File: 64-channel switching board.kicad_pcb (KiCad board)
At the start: 2 copper layers, 45.6 x 64.8 mm, 69 parts, among them P1 CONN_01X01, P10 CONN_01X01, P11 CONN_01X01, P12 CONN_01X01, P13 CONN_01X01, P14 CONN_01X01, P15 CONN_01X01, P16 CONN_01X01, P17 CONN_01X01, P18 CONN_01X01, P19 CONN_01X01, P2 CONN_01X01, P20 CONN_01X01, P21 CONN_01X01, P22 CONN_01X01, P23 CONN_01X01, P24 CONN_01X01, P25 CONN_01X01, P26 CONN_01X01, P27 CONN_01X01, P28 CONN_01X01, P29 CONN_01X01, P3 CONN_01X01, P30 CONN_01X01, P31 CONN_01X01, P32 CONN_01X01, P33 CONN_01X01, P34 CONN_01X01, P35 CONN_01X01, P36 CONN_01X01, P37 CONN_01X01, P38 CONN_01X01, P39 CONN_01X01, P4 CONN_01X01, P40 CONN_01X01, P41 CONN_01X01, P42 CONN_01X01, P43 CONN_01X01, P44 CONN_01X01, P45 CONN_01X01, P46 CONN_01X01, P47 CONN_01X01, P48 CONN_01X01, P49 CONN_01X01, P5 CONN_01X01, P50 CONN_01X01, P51 CONN_01X01, P52 CONN_01X01, P53 CONN_01X01, P54 CONN_01X01, P55 CONN_01X01, P56 CONN_01X01, P57 CONN_01X01, P58 CONN_01X01, P59 CONN_01X01, P6 CONN_01X01, P60 CONN_01X01, P61 CONN_01X01, P62 CONN_01X01, P63 CONN_01X01, P64 CONN_01X01, P65 CONN_01X10, P66 CONN_01X02, P7 CONN_01X01, P8 CONN_01X01, P9 CONN_01X01, U1 HV507

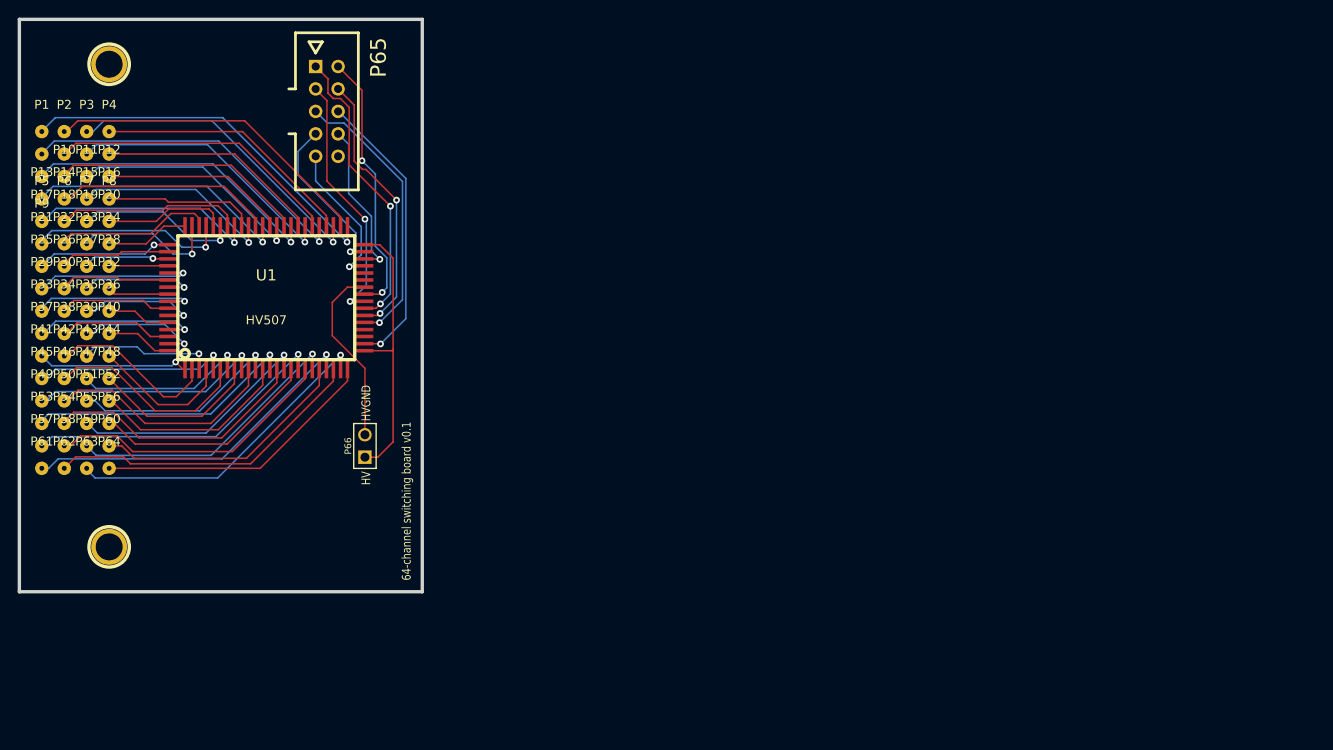
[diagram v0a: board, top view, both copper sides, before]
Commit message: Updated schematic and pcb to have 64 resistors and capacitors. Also added a version with 40 pin connector
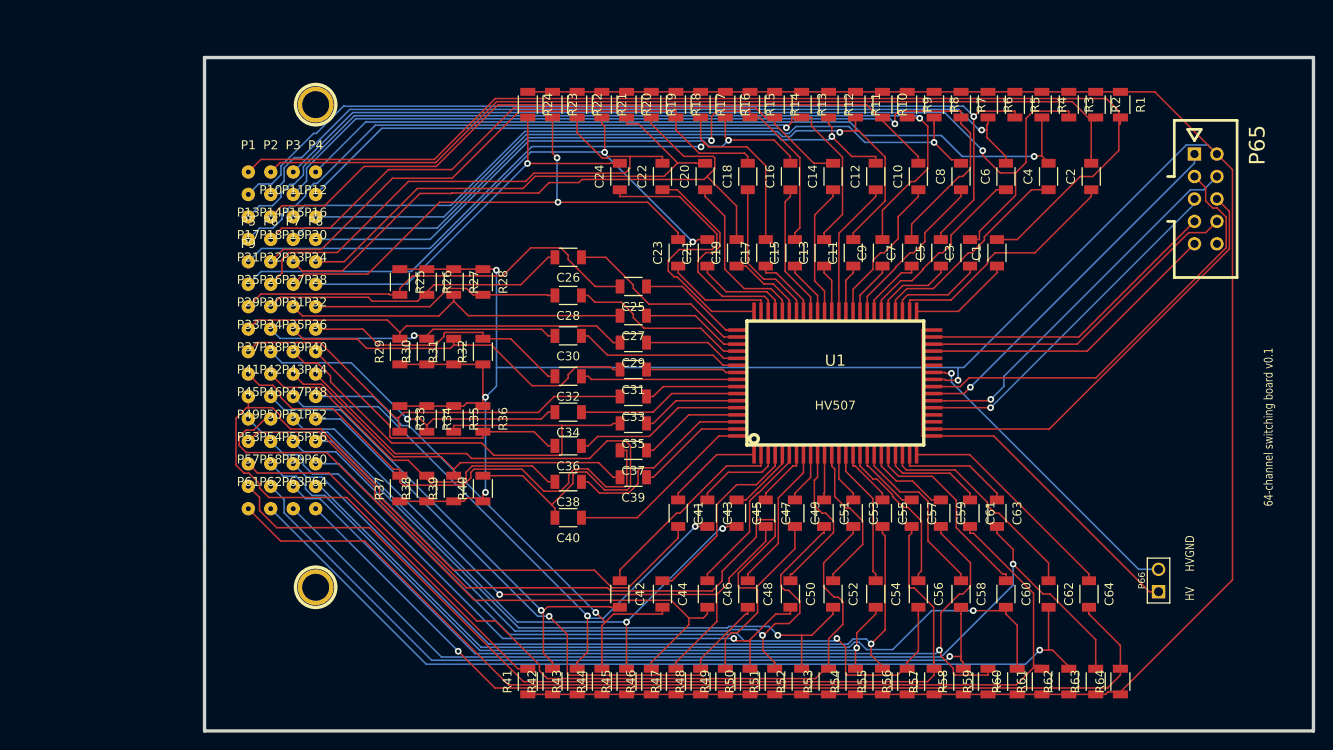
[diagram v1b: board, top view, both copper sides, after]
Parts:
- added C1: 3nF, Capacitors_SMD:C_1206, F.Cu at (123.2, 38.9)
- added C10: 3nF, Capacitors_SMD:C_1206, F.Cu at (114.3, 30.2)
- added C11: 3nF, Capacitors_SMD:C_1206, F.Cu at (106.9, 38.9)
- added C12: 3nF, Capacitors_SMD:C_1206, F.Cu at (109.5, 30.2)
- added C13: 3nF, Capacitors_SMD:C_1206, F.Cu at (103.6, 38.9)
- added C14: 3nF, Capacitors_SMD:C_1206, F.Cu at (104.6, 30.2)
- added C15: 3nF, Capacitors_SMD:C_1206, F.Cu at (100.3, 38.9)
- added C16: 3nF, Capacitors_SMD:C_1206, F.Cu at (99.8, 30.2)
- added C17: 3nF, Capacitors_SMD:C_1206, F.Cu at (97.0, 38.9)
- added C18: 3nF, Capacitors_SMD:C_1206, F.Cu at (95.0, 30.2)
- added C19: 3nF, Capacitors_SMD:C_1206, F.Cu at (93.7, 38.9)
- added C2: 3nF, Capacitors_SMD:C_1206, F.Cu at (133.9, 30.2)
- added C20: 3nF, Capacitors_SMD:C_1206, F.Cu at (90.2, 30.2)
- added C21: 3nF, Capacitors_SMD:C_1206, F.Cu at (90.4, 38.9)
- added C22: 3nF, Capacitors_SMD:C_1206, F.Cu at (85.3, 30.2)
- added C23: 3nF, Capacitors_SMD:C_1206, F.Cu at (87.1, 38.9)
- added C24: 3nF, Capacitors_SMD:C_1206, F.Cu at (80.5, 30.2)
- added C25: 3nF, Capacitors_SMD:C_1206, F.Cu at (82.0, 42.7)
- added C26: 3nF, Capacitors_SMD:C_1206, F.Cu at (74.7, 39.4)
- added C27: 3nF, Capacitors_SMD:C_1206, F.Cu at (82.0, 46.0)
- added C28: 3nF, Capacitors_SMD:C_1206, F.Cu at (74.7, 43.7)
- added C29: 3nF, Capacitors_SMD:C_1206, F.Cu at (82.0, 49.0)
- added C3: 3nF, Capacitors_SMD:C_1206, F.Cu at (120.1, 38.9)
- added C30: 3nF, Capacitors_SMD:C_1206, F.Cu at (74.7, 48.3)
- added C31: 3nF, Capacitors_SMD:C_1206, F.Cu at (82.0, 52.1)
- added C32: 3nF, Capacitors_SMD:C_1206, F.Cu at (74.7, 52.8)
- added C33: 3nF, Capacitors_SMD:C_1206, F.Cu at (82.0, 55.1)
- added C34: 3nF, Capacitors_SMD:C_1206, F.Cu at (74.7, 56.9)
- added C35: 3nF, Capacitors_SMD:C_1206, F.Cu at (82.0, 58.2)
- added C36: 3nF, Capacitors_SMD:C_1206, F.Cu at (74.7, 60.7)
- added C37: 3nF, Capacitors_SMD:C_1206, F.Cu at (82.0, 61.2)
- added C38: 3nF, Capacitors_SMD:C_1206, F.Cu at (74.7, 64.8)
- added C39: 3nF, Capacitors_SMD:C_1206, F.Cu at (82.0, 64.3)
- added C4: 3nF, Capacitors_SMD:C_1206, F.Cu at (129.0, 30.2)
- added C40: 3nF, Capacitors_SMD:C_1206, F.Cu at (74.7, 68.8)
- added C41: 3nF, Capacitors_SMD:C_1206, F.Cu at (87.1, 68.3)
- added C42: 3nF, Capacitors_SMD:C_1206, F.Cu at (80.5, 77.5)
- added C43: 3nF, Capacitors_SMD:C_1206, F.Cu at (90.4, 68.3)
- added C44: 3nF, Capacitors_SMD:C_1206, F.Cu at (85.3, 77.5)
- added C45: 3nF, Capacitors_SMD:C_1206, F.Cu at (93.7, 68.3)
- added C46: 3nF, Capacitors_SMD:C_1206, F.Cu at (90.4, 77.5)
- added C47: 3nF, Capacitors_SMD:C_1206, F.Cu at (97.0, 68.3)
- added C48: 3nF, Capacitors_SMD:C_1206, F.Cu at (95.0, 77.5)
- added C49: 3nF, Capacitors_SMD:C_1206, F.Cu at (100.3, 68.3)
- added C5: 3nF, Capacitors_SMD:C_1206, F.Cu at (116.8, 38.9)
- added C50: 3nF, Capacitors_SMD:C_1206, F.Cu at (99.8, 77.5)
- added C51: 3nF, Capacitors_SMD:C_1206, F.Cu at (103.6, 68.3)
- added C52: 3nF, Capacitors_SMD:C_1206, F.Cu at (104.6, 77.5)
- added C53: 3nF, Capacitors_SMD:C_1206, F.Cu at (106.9, 68.3)
- added C54: 3nF, Capacitors_SMD:C_1206, F.Cu at (109.5, 77.5)
- added C55: 3nF, Capacitors_SMD:C_1206, F.Cu at (110.2, 68.3)
- added C56: 3nF, Capacitors_SMD:C_1206, F.Cu at (114.3, 77.5)
- added C57: 3nF, Capacitors_SMD:C_1206, F.Cu at (113.5, 68.3)
- added C58: 3nF, Capacitors_SMD:C_1206, F.Cu at (119.1, 77.5)
- added C59: 3nF, Capacitors_SMD:C_1206, F.Cu at (116.8, 68.3)
- added C6: 3nF, Capacitors_SMD:C_1206, F.Cu at (124.2, 30.2)
- added C60: 3nF, Capacitors_SMD:C_1206, F.Cu at (124.2, 77.5)
- added C61: 3nF, Capacitors_SMD:C_1206, F.Cu at (120.1, 68.3)
- added C62: 3nF, Capacitors_SMD:C_1206, F.Cu at (129.0, 77.5)
- added C63: 3nF, Capacitors_SMD:C_1206, F.Cu at (123.2, 68.3)
- added C64: 3nF, Capacitors_SMD:C_1206, F.Cu at (133.6, 77.5)
- added C7: 3nF, Capacitors_SMD:C_1206, F.Cu at (113.5, 38.9)
- added C8: 3nF, Capacitors_SMD:C_1206, F.Cu at (119.1, 30.2)
- added C9: 3nF, Capacitors_SMD:C_1206, F.Cu at (110.2, 38.9)
- added R1: 510k, Resistors_SMD:R_1206, F.Cu at (137.2, 22.1)
- added R10: 510k, Resistors_SMD:R_1206, F.Cu at (110.2, 22.1)
- added R11: 510k, Resistors_SMD:R_1206, F.Cu at (107.2, 22.1)
- added R12: 510k, Resistors_SMD:R_1206, F.Cu at (104.1, 22.1)
- added R13: 510k, Resistors_SMD:R_1206, F.Cu at (101.1, 22.1)
- added R14: 510k, Resistors_SMD:R_1206, F.Cu at (98.0, 22.1)
- added R15: 510k, Resistors_SMD:R_1206, F.Cu at (95.2, 22.1)
- added R16: 510k, Resistors_SMD:R_1206, F.Cu at (92.5, 22.1)
- added R17: 510k, Resistors_SMD:R_1206, F.Cu at (89.7, 22.1)
- added R18: 510k, Resistors_SMD:R_1206, F.Cu at (86.9, 22.1)
- added R19: 510k, Resistors_SMD:R_1206, F.Cu at (84.1, 22.1)
- added R2: 510k, Resistors_SMD:R_1206, F.Cu at (134.4, 22.1)
- added R20: 510k, Resistors_SMD:R_1206, F.Cu at (81.3, 22.1)
- added R21: 510k, Resistors_SMD:R_1206, F.Cu at (78.5, 22.1)
- added R22: 510k, Resistors_SMD:R_1206, F.Cu at (75.7, 22.1)
- added R23: 510k, Resistors_SMD:R_1206, F.Cu at (72.9, 22.1)
- added R24: 510k, Resistors_SMD:R_1206, F.Cu at (70.1, 22.1)
- added R25: 510k, Resistors_SMD:R_1206, F.Cu at (55.6, 42.2)
- added R26: 510k, Resistors_SMD:R_1206, F.Cu at (58.7, 42.2)
- added R27: 510k, Resistors_SMD:R_1206, F.Cu at (61.7, 42.2)
- added R28: 510k, Resistors_SMD:R_1206, F.Cu at (65.0, 42.2)
- added R29: 510k, Resistors_SMD:R_1206, F.Cu at (55.6, 50.0)
- added R3: 510k, Resistors_SMD:R_1206, F.Cu at (131.3, 22.1)
- added R30: 510k, Resistors_SMD:R_1206, F.Cu at (58.7, 50.0)
- added R31: 510k, Resistors_SMD:R_1206, F.Cu at (61.7, 50.0)
- added R32: 510k, Resistors_SMD:R_1206, F.Cu at (65.0, 50.0)
- added R33: 510k, Resistors_SMD:R_1206, F.Cu at (55.6, 57.7)
- added R34: 510k, Resistors_SMD:R_1206, F.Cu at (58.7, 57.7)
- added R35: 510k, Resistors_SMD:R_1206, F.Cu at (61.7, 57.7)
- added R36: 510k, Resistors_SMD:R_1206, F.Cu at (65.0, 57.7)
- added R37: 510k, Resistors_SMD:R_1206, F.Cu at (55.6, 65.5)
- added R38: 510k, Resistors_SMD:R_1206, F.Cu at (58.7, 65.5)
- added R39: 510k, Resistors_SMD:R_1206, F.Cu at (61.7, 65.5)
- added R4: 510k, Resistors_SMD:R_1206, F.Cu at (128.3, 22.1)
- added R40: 510k, Resistors_SMD:R_1206, F.Cu at (65.0, 65.5)
- added R41: 510k, Resistors_SMD:R_1206, F.Cu at (70.1, 87.4)
- added R42: 510k, Resistors_SMD:R_1206, F.Cu at (72.9, 87.4)
- added R43: 510k, Resistors_SMD:R_1206, F.Cu at (75.7, 87.4)
- added R44: 510k, Resistors_SMD:R_1206, F.Cu at (78.5, 87.4)
- added R45: 510k, Resistors_SMD:R_1206, F.Cu at (81.3, 87.4)
- added R46: 510k, Resistors_SMD:R_1206, F.Cu at (84.1, 87.4)
- added R47: 510k, Resistors_SMD:R_1206, F.Cu at (86.9, 87.4)
- added R48: 510k, Resistors_SMD:R_1206, F.Cu at (89.7, 87.4)
- added R49: 510k, Resistors_SMD:R_1206, F.Cu at (92.5, 87.4)
- added R5: 510k, Resistors_SMD:R_1206, F.Cu at (125.2, 22.1)
- added R50: 510k, Resistors_SMD:R_1206, F.Cu at (95.2, 87.4)
- added R51: 510k, Resistors_SMD:R_1206, F.Cu at (98.0, 87.4)
- added R52: 510k, Resistors_SMD:R_1206, F.Cu at (101.1, 87.4)
- added R53: 510k, Resistors_SMD:R_1206, F.Cu at (104.1, 87.4)
- added R54: 510k, Resistors_SMD:R_1206, F.Cu at (107.2, 87.4)
- added R55: 510k, Resistors_SMD:R_1206, F.Cu at (110.2, 87.4)
- added R56: 510k, Resistors_SMD:R_1206, F.Cu at (113.0, 87.4)
- added R57: 510k, Resistors_SMD:R_1206, F.Cu at (116.1, 87.4)
- added R58: 510k, Resistors_SMD:R_1206, F.Cu at (119.4, 87.4)
- added R59: 510k, Resistors_SMD:R_1206, F.Cu at (122.2, 87.4)
- added R6: 510k, Resistors_SMD:R_1206, F.Cu at (122.2, 22.1)
- added R60: 510k, Resistors_SMD:R_1206, F.Cu at (125.5, 87.4)
- added R61: 510k, Resistors_SMD:R_1206, F.Cu at (128.3, 87.4)
- added R62: 510k, Resistors_SMD:R_1206, F.Cu at (131.3, 87.4)
- added R63: 510k, Resistors_SMD:R_1206, F.Cu at (134.4, 87.4)
- added R64: 510k, Resistors_SMD:R_1206, F.Cu at (137.2, 87.4)
- added R7: 510k, Resistors_SMD:R_1206, F.Cu at (119.1, 22.1)
- added R8: 510k, Resistors_SMD:R_1206, F.Cu at (116.1, 22.1)
- added R9: 510k, Resistors_SMD:R_1206, F.Cu at (113.0, 22.1)
- moved P65 99.9 mm to (146.8, 32.8)
- moved P66 91.1 mm to (141.5, 75.9)
- moved U1 65.1 mm to (104.9, 53.6)
- moved P1 23.8 mm to (38.5, 29.7)
- moved P10 23.8 mm to (41.0, 34.8)
- moved P13 23.8 mm to (38.5, 37.3)
- moved P14 23.8 mm to (41.0, 37.3)
- moved P17 23.8 mm to (38.5, 39.9)
- moved P18 23.8 mm to (41.0, 39.9)
- moved P2 23.8 mm to (41.0, 29.7)
- moved P21 23.8 mm to (38.5, 42.4)
- moved P22 23.8 mm to (41.0, 42.4)
- moved P25 23.8 mm to (38.5, 45.0)
- moved P26 23.8 mm to (41.0, 45.0)
- moved P29 23.8 mm to (38.5, 47.5)
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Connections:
- P1 pad 1: Net-(P1-Pad1) -> Net-(C1-Pad2)
- P10 pad 1: Net-(P10-Pad1) -> Net-(C10-Pad2)
- P11 pad 1: Net-(P11-Pad1) -> Net-(C11-Pad2)
- P12 pad 1: Net-(P12-Pad1) -> Net-(C12-Pad2)
- P13 pad 1: Net-(P13-Pad1) -> Net-(C13-Pad2)
- P14 pad 1: Net-(P14-Pad1) -> Net-(C14-Pad2)
- P15 pad 1: Net-(P15-Pad1) -> Net-(C15-Pad2)
- P16 pad 1: Net-(P16-Pad1) -> Net-(C16-Pad2)
- P17 pad 1: Net-(P17-Pad1) -> Net-(C17-Pad2)
- P18 pad 1: Net-(P18-Pad1) -> Net-(C18-Pad2)
- P19 pad 1: Net-(P19-Pad1) -> Net-(C19-Pad2)
- P2 pad 1: Net-(P2-Pad1) -> Net-(C2-Pad2)
- P20 pad 1: Net-(P20-Pad1) -> Net-(C20-Pad2)
- P21 pad 1: Net-(P21-Pad1) -> Net-(C21-Pad2)
- P22 pad 1: Net-(P22-Pad1) -> Net-(C22-Pad2)
- P23 pad 1: Net-(P23-Pad1) -> Net-(C23-Pad2)
- P24 pad 1: Net-(P24-Pad1) -> Net-(C24-Pad2)
- P25 pad 1: Net-(P25-Pad1) -> Net-(C25-Pad2)
- P26 pad 1: Net-(P26-Pad1) -> Net-(C26-Pad2)
- P27 pad 1: Net-(P27-Pad1) -> Net-(C27-Pad2)
- P28 pad 1: Net-(P28-Pad1) -> Net-(C28-Pad2)
- P29 pad 1: Net-(P29-Pad1) -> Net-(C29-Pad2)
- P3 pad 1: Net-(P3-Pad1) -> Net-(C3-Pad2)
- P30 pad 1: Net-(P30-Pad1) -> Net-(C30-Pad2)
- P31 pad 1: Net-(P31-Pad1) -> Net-(C31-Pad2)
- P32 pad 1: Net-(P32-Pad1) -> Net-(C32-Pad2)
- P33 pad 1: Net-(P33-Pad1) -> Net-(C33-Pad2)
- P34 pad 1: Net-(P34-Pad1) -> Net-(C34-Pad2)
- P35 pad 1: Net-(P35-Pad1) -> Net-(C35-Pad2)
- P36 pad 1: Net-(P36-Pad1) -> Net-(C36-Pad2)
- P37 pad 1: Net-(P37-Pad1) -> Net-(C37-Pad2)
- P38 pad 1: Net-(P38-Pad1) -> Net-(C38-Pad2)
- P39 pad 1: Net-(P39-Pad1) -> Net-(C39-Pad2)
- P4 pad 1: Net-(P4-Pad1) -> Net-(C4-Pad2)
- P40 pad 1: Net-(P40-Pad1) -> Net-(C40-Pad2)
- P41 pad 1: Net-(P41-Pad1) -> Net-(C41-Pad2)
- P42 pad 1: Net-(P42-Pad1) -> Net-(C42-Pad2)
- P43 pad 1: Net-(P43-Pad1) -> Net-(C43-Pad2)
- P44 pad 1: Net-(P44-Pad1) -> Net-(C44-Pad2)
- P45 pad 1: Net-(P45-Pad1) -> Net-(C45-Pad2)
- P46 pad 1: Net-(P46-Pad1) -> Net-(C46-Pad2)
- P47 pad 1: Net-(P47-Pad1) -> Net-(C47-Pad2)
- P48 pad 1: Net-(P48-Pad1) -> Net-(C48-Pad2)
- P49 pad 1: Net-(P49-Pad1) -> Net-(C49-Pad2)
- P5 pad 1: Net-(P5-Pad1) -> Net-(C5-Pad2)
- P50 pad 1: Net-(P50-Pad1) -> Net-(C50-Pad2)
- P51 pad 1: Net-(P51-Pad1) -> Net-(C51-Pad2)
- P52 pad 1: Net-(P52-Pad1) -> Net-(C52-Pad2)
- P53 pad 1: Net-(P53-Pad1) -> Net-(C53-Pad2)
- P54 pad 1: Net-(P54-Pad1) -> Net-(C54-Pad2)
- P55 pad 1: Net-(P55-Pad1) -> Net-(C55-Pad2)
- P56 pad 1: Net-(P56-Pad1) -> Net-(C56-Pad2)
- P57 pad 1: Net-(P57-Pad1) -> Net-(C57-Pad2)
- P58 pad 1: Net-(P58-Pad1) -> Net-(C58-Pad2)
- P59 pad 1: Net-(P59-Pad1) -> Net-(C59-Pad2)
- P6 pad 1: Net-(P6-Pad1) -> Net-(C6-Pad2)
- P60 pad 1: Net-(P60-Pad1) -> Net-(C60-Pad2)
- P61 pad 1: Net-(P61-Pad1) -> Net-(C61-Pad2)
- P62 pad 1: Net-(P62-Pad1) -> Net-(C62-Pad2)
- P63 pad 1: Net-(P63-Pad1) -> Net-(C63-Pad2)
- P64 pad 1: Net-(P64-Pad1) -> Net-(C64-Pad2)
- P65 pad 10: (no net) -> Net-(P65-Pad10)
- P7 pad 1: Net-(P7-Pad1) -> Net-(C7-Pad2)
- P8 pad 1: Net-(P8-Pad1) -> Net-(C8-Pad2)
- P9 pad 1: Net-(P9-Pad1) -> Net-(C9-Pad2)
- U1 pad 1: Net-(P41-Pad1) -> Net-(C41-Pad1)
- U1 pad 10: Net-(P50-Pad1) -> Net-(C50-Pad1)
- U1 pad 11: Net-(P51-Pad1) -> Net-(C51-Pad1)
- U1 pad 12: Net-(P52-Pad1) -> Net-(C52-Pad1)
- U1 pad 13: Net-(P53-Pad1) -> Net-(C53-Pad1)
- U1 pad 14: Net-(P54-Pad1) -> Net-(C54-Pad1)
- U1 pad 15: Net-(P55-Pad1) -> Net-(C55-Pad1)
- U1 pad 16: Net-(P56-Pad1) -> Net-(C56-Pad1)
- U1 pad 17: Net-(P57-Pad1) -> Net-(C57-Pad1)
- U1 pad 18: Net-(P58-Pad1) -> Net-(C58-Pad1)
- U1 pad 19: Net-(P59-Pad1) -> Net-(C59-Pad1)
- U1 pad 2: Net-(P42-Pad1) -> Net-(C42-Pad1)
- U1 pad 20: Net-(P60-Pad1) -> Net-(C60-Pad1)
- U1 pad 21: Net-(P61-Pad1) -> Net-(C61-Pad1)
- U1 pad 22: Net-(P62-Pad1) -> Net-(C62-Pad1)
- U1 pad 23: Net-(P63-Pad1) -> Net-(C63-Pad1)
- U1 pad 24: Net-(P64-Pad1) -> Net-(C64-Pad1)
- U1 pad 27: (no net) -> Net-(U1-Pad27)
- U1 pad 28: (no net) -> Net-(U1-Pad28)
- U1 pad 3: Net-(P43-Pad1) -> Net-(C43-Pad1)
- U1 pad 35: (no net) -> Net-(U1-Pad35)
- U1 pad 36: (no net) -> Net-(U1-Pad36)
- U1 pad 4: Net-(P44-Pad1) -> Net-(C44-Pad1)
- U1 pad 41: Net-(P1-Pad1) -> Net-(C1-Pad1)
- U1 pad 42: Net-(P2-Pad1) -> Net-(C2-Pad1)
- U1 pad 43: Net-(P3-Pad1) -> Net-(C3-Pad1)
- U1 pad 44: Net-(P4-Pad1) -> Net-(C4-Pad1)
- U1 pad 45: Net-(P5-Pad1) -> Net-(C5-Pad1)
- U1 pad 46: Net-(P6-Pad1) -> Net-(C6-Pad1)
- U1 pad 47: Net-(P7-Pad1) -> Net-(C7-Pad1)
- U1 pad 48: Net-(P8-Pad1) -> Net-(C8-Pad1)
- U1 pad 49: Net-(P9-Pad1) -> Net-(C9-Pad1)
- U1 pad 5: Net-(P45-Pad1) -> Net-(C45-Pad1)
- U1 pad 50: Net-(P10-Pad1) -> Net-(C10-Pad1)
- U1 pad 51: Net-(P11-Pad1) -> Net-(C11-Pad1)
- U1 pad 52: Net-(P12-Pad1) -> Net-(C12-Pad1)
- U1 pad 53: Net-(P13-Pad1) -> Net-(C13-Pad1)
- U1 pad 54: Net-(P14-Pad1) -> Net-(C14-Pad1)
- U1 pad 55: Net-(P15-Pad1) -> Net-(C15-Pad1)
- U1 pad 56: Net-(P16-Pad1) -> Net-(C16-Pad1)
- U1 pad 57: Net-(P17-Pad1) -> Net-(C17-Pad1)
- U1 pad 58: Net-(P18-Pad1) -> Net-(C18-Pad1)
- U1 pad 59: Net-(P19-Pad1) -> Net-(C19-Pad1)
- U1 pad 6: Net-(P46-Pad1) -> Net-(C46-Pad1)
- U1 pad 60: Net-(P20-Pad1) -> Net-(C20-Pad1)
- U1 pad 61: Net-(P21-Pad1) -> Net-(C21-Pad1)
- U1 pad 62: Net-(P22-Pad1) -> Net-(C22-Pad1)
- U1 pad 63: Net-(P23-Pad1) -> Net-(C23-Pad1)
- U1 pad 64: Net-(P24-Pad1) -> Net-(C24-Pad1)
- U1 pad 65: Net-(P25-Pad1) -> Net-(C25-Pad1)
- U1 pad 66: Net-(P26-Pad1) -> Net-(C26-Pad1)
- U1 pad 67: Net-(P27-Pad1) -> Net-(C27-Pad1)
- U1 pad 68: Net-(P28-Pad1) -> Net-(C28-Pad1)
- U1 pad 69: Net-(P29-Pad1) -> Net-(C29-Pad1)
- U1 pad 7: Net-(P47-Pad1) -> Net-(C47-Pad1)
- U1 pad 70: Net-(P30-Pad1) -> Net-(C30-Pad1)
- U1 pad 71: Net-(P31-Pad1) -> Net-(C31-Pad1)
- U1 pad 72: Net-(P32-Pad1) -> Net-(C32-Pad1)
- U1 pad 73: Net-(P33-Pad1) -> Net-(C33-Pad1)
- U1 pad 74: Net-(P34-Pad1) -> Net-(C34-Pad1)
- U1 pad 75: Net-(P35-Pad1) -> Net-(C35-Pad1)
- U1 pad 76: Net-(P36-Pad1) -> Net-(C36-Pad1)
- U1 pad 77: Net-(P37-Pad1) -> Net-(C37-Pad1)
- U1 pad 78: Net-(P38-Pad1) -> Net-(C38-Pad1)
- U1 pad 79: Net-(P39-Pad1) -> Net-(C39-Pad1)
- U1 pad 8: Net-(P48-Pad1) -> Net-(C48-Pad1)
- U1 pad 80: Net-(P40-Pad1) -> Net-(C40-Pad1)
- U1 pad 9: Net-(P49-Pad1) -> Net-(C49-Pad1)
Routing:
- net GND: track 30.2 -> 383.1 mm, vias 2 -> 4
- net Net-(C1-Pad2): track 0.00 -> 125.9 mm
- net Net-(C61-Pad2): track 0.00 -> 118.4 mm
- net Net-(C63-Pad2): track 0.00 -> 115.4 mm, vias 0 -> 1
- net Net-(C41-Pad2): track 0.00 -> 112.8 mm
- net Net-(C3-Pad2): track 0.00 -> 110.5 mm, vias 0 -> 1
- net Net-(C64-Pad2): track 0.00 -> 109.2 mm, vias 0 -> 1
- net Net-(C5-Pad2): track 0.00 -> 108.4 mm, vias 0 -> 1
- net Net-(C57-Pad2): track 0.00 -> 106.3 mm
- net Net-(C59-Pad2): track 0.00 -> 106.2 mm, vias 0 -> 1
- net Net-(C49-Pad2): track 0.00 -> 104.3 mm
- net Net-(C62-Pad2): track 0.00 -> 104.1 mm, vias 0 -> 1
- net Net-(C2-Pad2): track 0.00 -> 102.7 mm
- net Net-(C9-Pad2): track 0.00 -> 99.6 mm, vias 0 -> 1
- net Net-(C7-Pad2): track 0.00 -> 99.3 mm, vias 0 -> 1
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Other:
- board size 45.6 x 64.8 mm -> 125.5 x 76.2 mm
